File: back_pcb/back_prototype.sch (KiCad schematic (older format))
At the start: 27 parts, among them U1 Pi0Top

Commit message: Started new back PCB
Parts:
- removed W10: RXD, Measurement_Points:Measurement_Point_Square-SMD-Pad_Small, symbol TEST_1P
- removed W13: SDA, Measurement_Points:Measurement_Point_Square-SMD-Pad_Small, symbol TEST_1P
- removed W14: SCL, Measurement_Points:Measurement_Point_Square-SMD-Pad_Small, symbol TEST_1P
- removed W15: MOSI, Measurement_Points:Measurement_Point_Square-SMD-Pad_Small, symbol TEST_1P
- removed W16: MISO, Measurement_Points:Measurement_Point_Square-SMD-Pad_Small, symbol TEST_1P
- removed W17: SCK, Measurement_Points:Measurement_Point_Square-SMD-Pad_Small, symbol TEST_1P
- removed W18: TEST_1P, Measurement_Points:Measurement_Point_Square-SMD-Pad_Small, symbol TEST_1P
- removed W19: CS1, Measurement_Points:Measurement_Point_Square-SMD-Pad_Small, symbol TEST_1P
- removed W20: GP4, Measurement_Points:Measurement_Point_Square-SMD-Pad_Small, symbol TEST_1P
- removed W21: GP17, Measurement_Points:Measurement_Point_Square-SMD-Pad_Small, symbol TEST_1P
- removed W22: GP12, Measurement_Points:Measurement_Point_Square-SMD-Pad_Small, symbol TEST_1P
- removed W23: GP16, Measurement_Points:Measurement_Point_Square-SMD-Pad_Small, symbol TEST_1P
- removed W24: GP20, Measurement_Points:Measurement_Point_Square-SMD-Pad_Small, symbol TEST_1P
- removed W25: GP21, Measurement_Points:Measurement_Point_Square-SMD-Pad_Small, symbol TEST_1P
- removed W26, W5, W6, W7, W8: GND, Measurement_Points:Measurement_Point_Square-SMD-Pad_Small, symbol TEST_1P
- removed W3: RST, Measurement_Points:Measurement_Point_Square-SMD-Pad_Small, symbol TEST_1P
- removed W4: TV_OUT, Measurement_Points:Measurement_Point_Square-SMD-Pad_Small, symbol TEST_1P
- removed W9: TXD, Measurement_Points:Measurement_Point_Square-SMD-Pad_Small, symbol TEST_1P
- added C13, C14, C15, C25, C4, C5, C6, C7, C8: C_Small, Capacitors_SMD:C_0805, symbol C_Small
- added C16, C17, C18, C19, C20, C21, C22, C23, C24: C_Small, Capacitors_SMD:C_0603, symbol C_Small
- added D?: Led_RGB_CA, symbol Led_RGB_CA
- added D?: LED, symbol LED
- added JP? (x4): JUMPER3, symbol JUMPER3
- added P5: CONN_01X04, Pin_Headers:Pin_Header_Straight_1x04_Pitch2.54mm, symbol CONN_01X04
- added P6: CONN_01X07, Pin_Headers:Pin_Header_Straight_1x07_Pitch2.54mm, symbol CONN_01X07
- added R? (x6): R, symbol R
- added U?: SIM800_BREAKOUT, symbol SIM800_BREAKOUT
- added U?: MCP23017, symbol MCP23017
- added W? (x21): TEST_1P, Measurement_Points:Measurement_Point_Square-SMD-Pad_Small, symbol TEST_1P
- U1: footprint Pi0Top:Pi0Top -> common-footprints:pi0outline
- W12: value GND -> TEST_1P
- W2: value GP1 -> TEST_1P
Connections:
- net +3V3: now also C13.1, C14.1, C15.1, C25.1, C4.1, C5.1, C6.1, C7.1, C8.1, JP?.1, JP?.1, JP?.3, JP?.3, P6.7 (P7), U?.9 (VCC); no longer W1.1
- net GND: now also C13.2, C14.2, C15.2, C16.1, C18.2, C19.1, C21.2, C22.1, C24.2, C25.2, C4.2, C5.2, C6.2, C7.2, C8.2, D?.1 (K), JP?.1, JP?.1, JP?.2, JP?.2, JP?.2, JP?.3, P6.1 (P1), R?.2, U?.10 (GND), U?.15 (A0), U?.16 (A1), U?.17 (A2), U?.5 (GND); no longer U1.44 (GND)
- net VPP: now also U?.1 (VBAT)
- net SIM800_TXD: now reaches U1.10 (GP15/RXD)
- net SIM800_TXD: now also W2.1, U?.4 (TXD)
- net at U1.19 (GP10/MOSI): now also W?.1
- net at U1.21 (GP9/MISO): now also W?.1
- net at U1.23 (GP11/SSCK): now also W?.1
- net at U1.24 (GP8/CS0): now also W?.1
- net at U1.26 (GP7/CS1): now also W?.1
- net MCP_INT: now reaches U1.28 (ID_SC)
- net MCP_INT: now also U?.19 (INTB), U?.20 (INTA); no longer W2.1
- net SDA: now reaches U1.3 (GP2/SDA)
- net SDA: now also U?.13 (SDA)
- net at U1.32 (GP12): now also W?.1
- net at U1.35 (GP19): now also W?.1
- net at U1.36 (GP16): now also W?.1
- net at U1.38 (GP20): now also W?.1
- net at U1.42 (RST): now also W?.1
- net at U1.43 (TV_OUT): now also W?.1
- net SCL: now reaches U1.5 (GP3/SCL)
- net SCL: now also U?.12 (SCL)
- net at U1.7 (GP4): now also W?.1
- net SIM800_RXD: now reaches U1.8 (GP14/TXD)
- net SIM800_RXD: now also W1.1, U?.3 (RXD)
- new net: U1.44 (GND), W?.1
- new net: U?.25 (PA4), W?.1
- new net: U?.26 (PA5), W?.1
- new net: U?.27 (PA6), W?.1
- new net: U?.28 (PA7), W?.1
- new net: D?.1, JP?.2
- new net: D?.2 (R), R?.1
- new net: D?.3 (G), R?.1
- new net: D?.4 (B), R?.1
- new net: D?.2 (A), R?.1
- new net +5V: R?.1
- new net ATMEGA_ADC: P6.5 (P5)
- new net ATMEGA_GPIO: P6.6 (P6)
- new net ATMEGA_RST: P6.2 (P2)
- new net ATMEGA_RXD: P6.3 (P3)
- new net ATMEGA_TXD: P6.4 (P4)
- new net CHARGING_SENSE: R?.1, R?.2, U?.8 (PB7)
- new net FLASH_LED: R?.2, U?.24 (PA3), W?.1
- new net MIC+: C16.2, C17.1, C22.2, C23.1, P5.1 (P1), U?.8 (MIC+)
- new net MIC-: C17.2, C18.1, C23.2, C24.1, P5.2 (P2), U?.9 (MIC-)
- new net NOTIF_LED_B: R?.2, U?.23 (PA2), W?.1
- new net NOTIF_LED_G: R?.2, U?.22 (PA1), W?.1
- new net NOTIF_LED_R: R?.2, U?.21 (PA0), W?.1
- new net SIM800_DTR: U?.2 (PB1), U?.7 (DTR)
- new net SIM800_RING: U?.1 (PB0), U?.6 (RING)
- new net SIM800_RST: U?.2 (RST), U?.3 (PB2)
- new net SPK+: C19.2, C20.1, P5.4 (P4), U?.10 (SPK+)
- new net SPK-: C20.2, C21.1, P5.3 (P3), U?.11 (SPK-)
- no-connect marks 14 -> 17
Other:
- moved on the sheet: U1, W11, W12

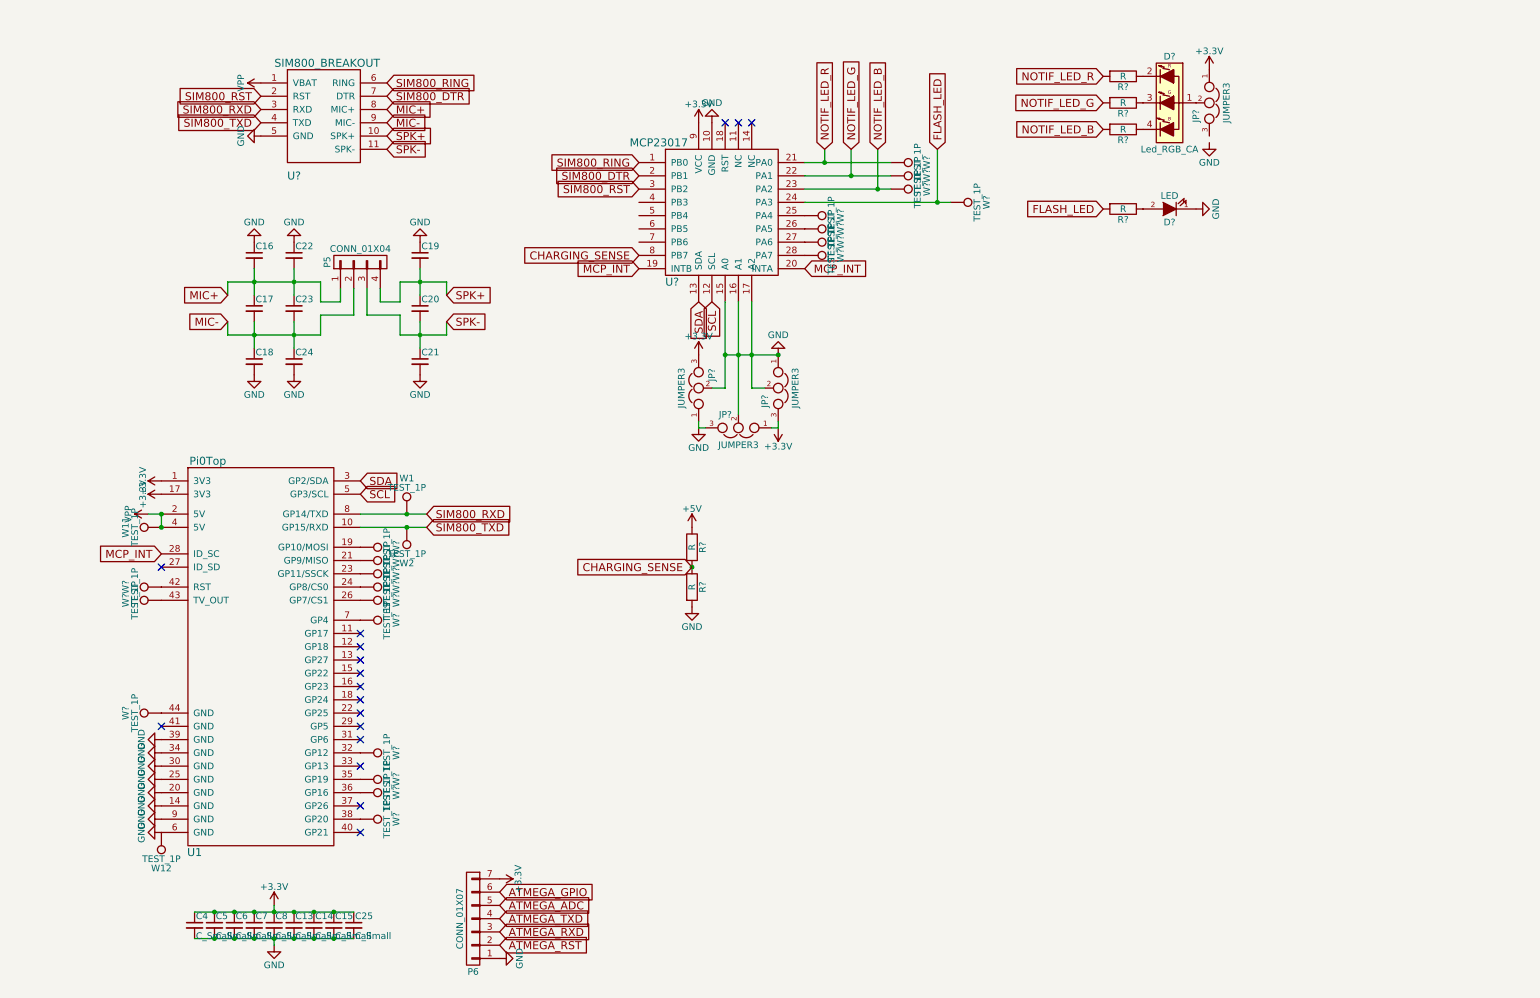
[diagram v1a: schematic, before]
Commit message: Some more schematic work on back PCB
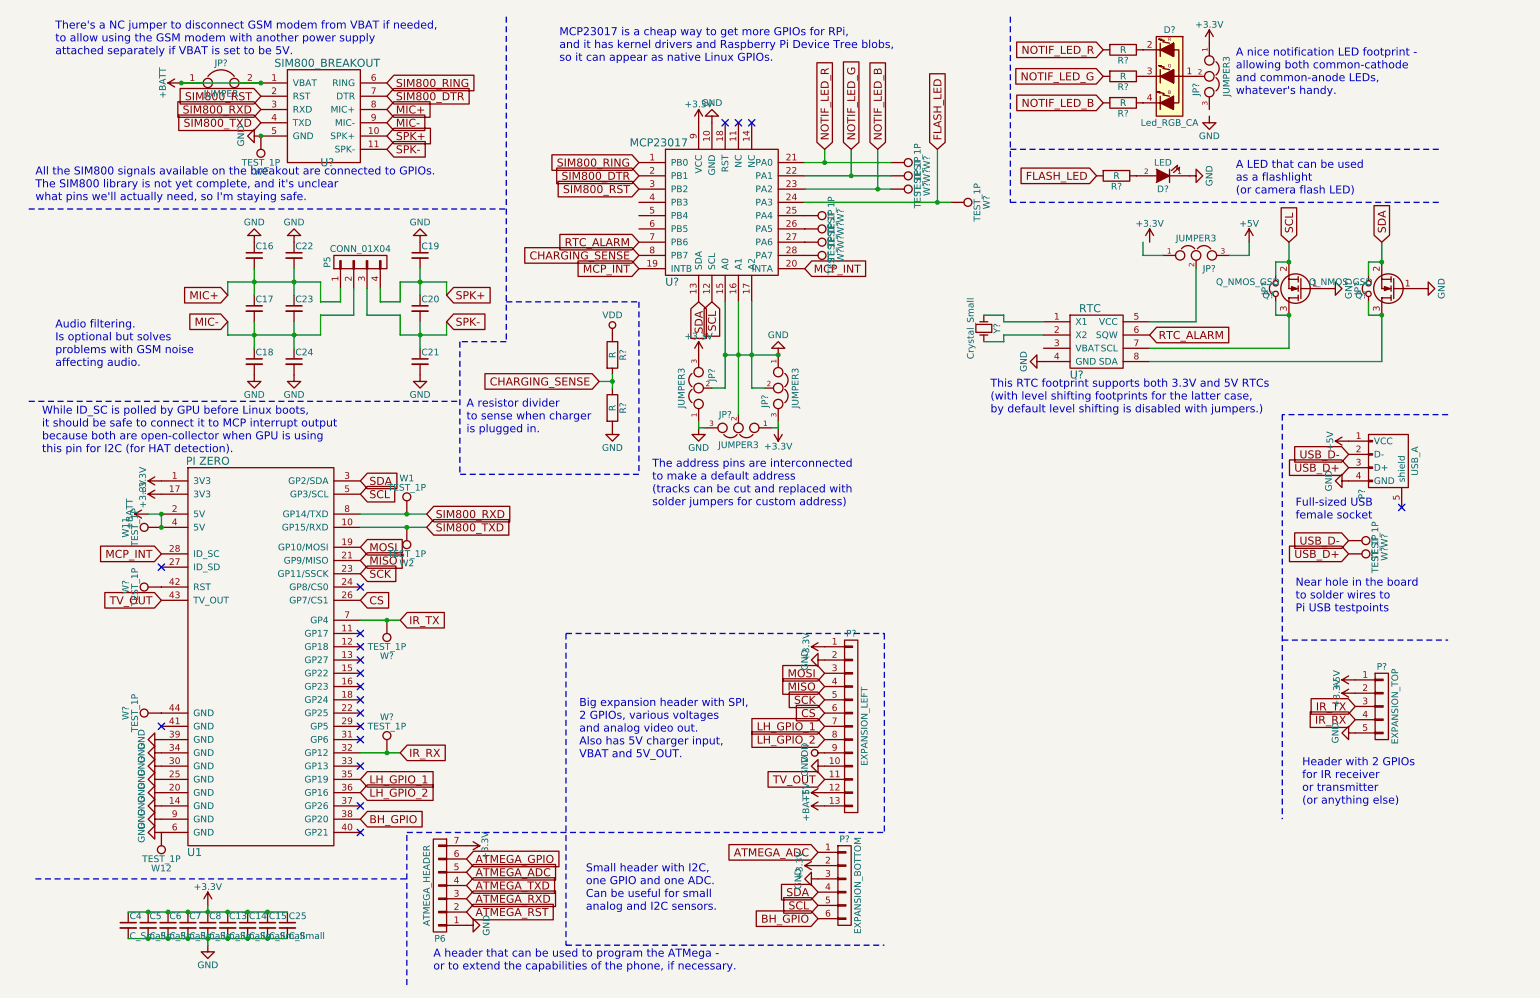
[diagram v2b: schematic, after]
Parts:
- removed W? (x10): TEST_1P, Measurement_Points:Measurement_Point_Square-SMD-Pad_Small, symbol TEST_1P
- added JP?: JUMPER3, symbol JUMPER3
- added JP? (x2): Jumper_NC_Small, symbol Jumper_NC_Small
- added JP?: JUMPER, symbol JUMPER
- added P?: EXPANSION_TOP, symbol CONN_01X05
- added P?: EXPANSION_BOTTOM, symbol CONN_01X06
- added P?: USB_A, symbol USB_A
- added P?: EXPANSION_LEFT, symbol CONN_01X13
- added Q? (x2): Q_NMOS_GSD, symbol Q_NMOS_GSD
- added U?: RTC, symbol RTC
- added W? (x4): TEST_1P, Measurement_Points:Measurement_Point_Square-SMD-Pad_Small, symbol TEST_1P
- added Y?: Crystal_Small, symbol Crystal_Small
- P6: value CONN_01X07 -> ATMEGA_HEADER
- U1: value Pi0Top -> PI ZERO
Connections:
- net +3V3: now also P?.1 (P1), P?.2 (P2), P?.2 (P2)
- net +5V: now also JP?.3, P?.1 (P1), P?.1 (VCC), P?.12 (P12); no longer R?.1
- net ATMEGA_ADC: now also P?.1 (P1)
- net GND: now also P?.10 (P10), P?.2 (P2), P?.3 (P3), P?.4 (GND), P?.5 (P5), Q?.1 (G), Q?.1 (G), U?.4 (GND), W?.1
- net SCL: now also JP?.2, P?.5 (P5), Q?.2 (S)
- net SDA: now also JP?.2, P?.4 (P4), Q?.2 (S)
- net MOSI: now reaches U1.19 (GP10/MOSI)
- net MOSI: now also P?.3 (P3)
- net MISO: now reaches U1.21 (GP9/MISO)
- net MISO: now also P?.4 (P4)
- net SCK: now reaches U1.23 (GP11/SSCK)
- net SCK: now also P?.5 (P5)
- net CS: now reaches U1.26 (GP7/CS1)
- net CS: now also P?.6 (P6)
- net IR_RX: now reaches U1.32 (GP12)
- net IR_RX: now also P?.4 (P4), W?.1
- net LH_GPIO_1: now reaches U1.35 (GP19)
- net LH_GPIO_1: now also P?.7 (P7)
- net LH_GPIO_2: now reaches U1.36 (GP16)
- net LH_GPIO_2: now also P?.8 (P8)
- net BH_GPIO: now reaches U1.38 (GP20)
- net BH_GPIO: now also P?.6 (P6)
- net TV_OUT: now reaches U1.43 (TV_OUT)
- net TV_OUT: now also P?.11 (P11)
- net IR_TX: now reaches U1.7 (GP4), W?.1
- net IR_TX: now also P?.3 (P3)
- net RTC_ALARM: now reaches U?.7 (PB6)
- net RTC_ALARM: now also U?.6 (SQW)
- net VPP renamed +BATT
- net +BATT: now also JP?.1, JP?.2, P?.13 (P13)
- new net: U?.1 (X1), Y?.1
- new net: U?.2 (X2), Y?.2
- new net: JP?.2, U?.5 (VCC)
- new net: JP?.1, Q?.3 (D), U?.7 (SCL)
- new net: JP?.1, Q?.3 (D), U?.8 (SDA)
- new net USB_D+: P?.3 (D+), W?.1
- new net USB_D-: P?.2 (D-), W?.1
- new net VDD: P?.9 (P9), R?.1
- no-connect marks 17 -> 19
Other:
- note added: "A LED that can be used \nas a flashlight \n(or camera flash LED)"
- note added: "A header that can be used to program the ATMega - \nor to extend the capabilities of the phone, if necessary."
- note added: "A nice notification LED footprint -\nallowing both common-cathode\nand common-anode LEDs,\nwhatever's handy."
- note added: "A resistor divider\nto sense when charger \nis plugged in."
- note added: "All the SIM800 signals available on the breakout are connected to GPIOs.\nThe SIM800 library is not yet complete, and it's unclear\nwhat pins we'll actually need, so I'm staying safe."
- note added: "Audio filtering.\nIs optional but solves \nproblems with GSM noise\naffecting audio."
- note added: "Big expansion header with SPI,\n2 GPIOs, various voltages\nand analog video out.\nAlso has 5V charger input,\nVBAT and 5V_OUT."
- note added: "Full-sized USB \nfemale socket"
- note added: "Header with 2 GPIOs\nfor IR receiver \nor transmitter\n(or anything else)"
- note added: "MCP23017 is a cheap way to get more GPIOs for RPi,\nand it has kernel drivers and Raspberry Pi Device Tree blobs,\nso it can appear as native Linux GPIOs."
- note added: "Near hole in the board\nto solder wires to \nPi USB testpoints"
- note added: "Small header with I2C, \none GPIO and one ADC. \nCan be useful for small \nanalog and I2C sensors."
- note added: "The address pins are interconnected\nto make a default address \n(tracks can be cut and replaced with\nsolder jumpers for custom address)"
- note added: "There's a NC jumper to disconnect GSM modem from VBAT if needed,\nto allow using the GSM modem with another power supply \nattached separately if VBAT is set to be 5V."
- note added: "This RTC footprint supports both 3.3V and 5V RTCs\n(with level shifting footprints for the latter case,\nby default level shifting is disabled with jumpers.)"
- note added: "While ID_SC is polled by GPU before Linux boots, \nit should be safe to connect it to MCP interrupt output \nbecause both are open-collector when GPU is using\nthis pin for I2C (for HAT detection)."
- moved on the sheet: C13, C14, C15, C25, C4, C5, C6, C7, C8, D?, JP?, P6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

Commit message: Beautiful annotations
So fabulous
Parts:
- added R? (x2): R, symbol R
- added W? (x4): TEST_1P, Measurement_Points:Measurement_Point_Square-SMD-Pad_Small, symbol TEST_1P
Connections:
- net ATMEGA_GPIO: now also W?.1
- net ATMEGA_RST: now also W?.1
- net ATMEGA_RXD: now also W?.1
- net ATMEGA_TXD: now also W?.1
- net at JP?.2, U?.5 (VCC): now also R?.1, R?.2
- net at JP?.1, Q?.3 (D), U?.7 (SCL): now also R?.2
- net at JP?.1, Q?.3 (D), U?.8 (SDA): now also R?.1
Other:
- note added: "ATMega programming \nheader"
- moved on the sheet: JP?, Q?

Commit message: Back board almost finished
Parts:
- removed P?: EXPANSION_BOTTOM, symbol CONN_01X06
- added D1: D_Small, Diodes_SMD:D_MiniMELF_Handsoldering, symbol D_Small
- added JP1, JP5: JUMPER, Connect:GS2, symbol JUMPER
- added P2: EXPANSION_BOTTOM, Pin_Headers:Pin_Header_Angled_1x04_Pitch2.54mm, symbol CONN_01X04
- added P7: EXPANSION_BOTTOM2, Pin_Headers:Pin_Header_Angled_1x02_Pitch2.54mm, symbol CONN_01X02
- added P8: CONN_01X02, footprints:JST_PH_S2B-PH-SM4-TB_02x2.00mm_Angled, symbol CONN_01X02
- added Q1, Q?: Q_PMOS_GSD, TO_SOT_Packages_SMD:SOT-23_Handsoldering, symbol Q_PMOS_GSD
- added R3, R?: R, Resistors_SMD:R_0805_HandSoldering, symbol R
- added U4: TP4056_BREAKOUT, footprints:TP4056_BREAKOUT, symbol TP4056_BREAKOUT
- added U?: DC_DC_BREAKOUT, symbol DC_DC_BREAKOUT
- added W14, W27, W28, W29: TEST_1P, Measurement_Points:Measurement_Point_Square-SMD-Pad_Small, symbol TEST_1P
- added W15: BAT-, Measurement_Points:Measurement_Point_Square-SMD-Pad_Small, symbol TEST_1P
- added W16: BAT+, Measurement_Points:Measurement_Point_Square-SMD-Pad_Small, symbol TEST_1P
- JP10, JP2, JP9: renamed from JP?; footprint (none) -> Connect:GS2
- JP3, JP4, JP6, JP7, JP8: renamed from JP?; footprint (none) -> Connect:GS3
- P1: renamed from P?; footprint (none) -> Pin_Headers:Pin_Header_Angled_1x13_Pitch2.54mm
- P3: renamed from P?; footprint (none) -> Pin_Headers:Pin_Header_Angled_1x05_Pitch2.54mm
- P4: renamed from P?; footprint (none) -> Connect:USB_A
- Q2, Q3: renamed from Q?; footprint (none) -> TO_SOT_Packages_SMD:SOT-23_Handsoldering
- R1, R2, R4, R5, R6, R7, R8, R9: renamed from R?; footprint (none) -> Resistors_SMD:R_0805_HandSoldering
- U2: renamed from U?; footprint (none) -> footprints:SIM800_BREAKOUT
- U3: renamed from U?; footprint (none) -> SMD_Packages:SOIC-28
- U5: renamed from U?; footprint (none) -> Housings_SOIC:SOIC-8_3.9x4.9mm_Pitch1.27mm
- W11: value TEST_1P -> BAT_IN
- Y1: renamed from Y?; footprint (none) -> Crystals:Crystal_SMD_G8-2pin_3.2x1.5mm_HandSoldering
- gave numbers to parts that had none: 21
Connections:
- net +3V3: now also JP7.1, JP7.2, P1.13 (P13), R8.1, R9.2, U5.5 (VCC), P2.1 (P1); no longer P1.1 (P1), P6.7 (P7)
- net +5V: now also P1.2 (P2), U?.4 (+5V); no longer P1.12 (P12)
- net +BATT: now also P1.1 (P1), JP1.1, JP1.2, P8.1 (P1), Q1.3 (D), Q?.3 (D), R?.2, U4.3 (VBAT), U4.4 (B+), W16.1; no longer JP2.1, JP2.2, P1.13 (P13), U1.2 (5V), U1.4 (5V)
- net ATMEGA_ADC: now also P7.2 (P2), W29.1
- net BH_GPIO: now also P7.1 (P1)
- net CS: now also P1.8 (P8); no longer P1.6 (P6)
- net FLASH_LED: now also U3.25 (PA4), W17.1; no longer U3.24 (PA3), W24.1
- net GND: now also JP8.3, P1.12 (P12), P1.4 (P4), JP5.2, P2.2 (P2), R3.2, U4.2 (GND), U4.6 (GND), U?.1 (GND), U?.3 (GND), W14.1; no longer P1.10 (P10), P1.2 (P2)
- net LH_GPIO_2: now also P1.6 (P6); no longer P1.8 (P8)
- net MCP_INT: now also W28.1
- net MISO: now also P1.10 (P10); no longer P1.4 (P4)
- net MOSI: now also P1.11 (P11); no longer P1.3 (P3)
- net NOTIF_LED_B: now also U3.26 (PA5), W18.1; no longer U3.23 (PA2), W23.1
- net NOTIF_LED_G: now also U3.27 (PA6), W19.1; no longer U3.22 (PA1), W22.1
- net NOTIF_LED_R: now also U3.28 (PA7), W20.1; no longer U3.21 (PA0), W21.1
- net RTC_ALARM: now also JP2.1; no longer U3.7 (PB6)
- net SCK: now also P1.9 (P9); no longer P1.5 (P5)
- net SCL: now also P2.4 (P4)
- net SDA: now also P2.3 (P3)
- net SIM800_DTR: now also U3.1 (PB0); no longer U3.2 (PB1)
- net SIM800_RING: now also U3.2 (PB1); no longer U3.1 (PB0)
- net TV_OUT: now also P1.3 (P3); no longer P1.11 (P11)
- net VDD: now also P1.5 (P5), D1.2 (A), Q1.1 (G), R3.1, U4.1 (CHRG); no longer P1.9 (P9)
- net PI_RST: now reaches U1.42 (RST), W3.1
- net DCDC_EN: now reaches U3.6 (PB5)
- net DCDC_EN: now also Q?.1 (G), R?.1
- new net: P6.7 (P7), W27.1
- new net: U3.21 (PA0), W21.1
- new net: U3.22 (PA1), W22.1
- new net: U3.23 (PA2), W23.1
- new net: U3.24 (PA3), W24.1
- new net: JP2.2, U3.7 (PB6)
- new net: Q?.2 (S), U?.2 (VIN)
- new net BATT-: JP5.1, P8.2 (P2), U4.5 (B-), W15.1
- new net VPP: D1.1 (K), Q1.2 (S), U1.2 (5V), U1.4 (5V)
- no-connect marks 19 -> 21
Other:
- note added: "A header that can be used to program the ATMega - \nor to extend the capabilities of the phone, if necessary.\n3.3V is not connected, but brought on a testpoint."
- note added: "Big expansion header \nwith SPI, 2 GPIOs, \nvarious voltages and \nanalog video out.\nAlso has 5V charger \ninput, VBAT and 5V_OUT."
- note added: "MCP23017 is a cheap way to get more GPIOs \nfor RPi, and it has kernel drivers and \nRaspberry Pi Device Tree blobs, so it can \nappear as native Linux GPIOs."
- note added: "Pins on testpoints"
- note added: "Small headers with I2C, \none GPIO and one ADC. \nCan be useful for small \nanalog and I2C sensors."
- note added: "The address pins are \ninterconnected for a default \naddress (tracks can be cut \nand jumpered for custom \naddress)"
- note added: "The board has a hole,\nyou solder wires from\nthese testpoints to\nPi USB testpoints\nthrough the hole"
- note added: "This simple P-FET circuit \nswitches Pi Zero power from \nbattery to 5V in when phone's \ncharging. It lets the battery\ncharge fully and more quickly. \nThe GSM modem is the only \nthing powered by VBAT all the \ntime (doesn't support 5V)."
- note removed: "A header that can be used to program the ATMega - \nor to extend the capabilities of the phone, if necessary."
- note removed: "ATMega programming \nheader"
- note removed: "Big expansion header with SPI,\n2 GPIOs, various voltages\nand analog video out.\nAlso has 5V charger input,\nVBAT and 5V_OUT."
- note removed: "MCP23017 is a cheap way to get more GPIOs for RPi,\nand it has kernel drivers and Raspberry Pi Device Tree blobs,\nso it can appear as native Linux GPIOs."
- note removed: "Near hole in the board\nto solder wires to \nPi USB testpoints"
- note removed: "Small header with I2C, \none GPIO and one ADC. \nCan be useful for small \nanalog and I2C sensors."
- note removed: "The address pins are interconnected\nto make a default address \n(tracks can be cut and replaced with\nsolder jumpers for custom address)"
- moved on the sheet: JP10, JP2, JP3, JP4, JP6, JP7, JP9, P1, Q2, Q3, R1, R2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
